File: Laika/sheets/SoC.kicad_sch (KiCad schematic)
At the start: 2 parts, among them J6 Conn_01x03, U1 Milk-V Duo Module

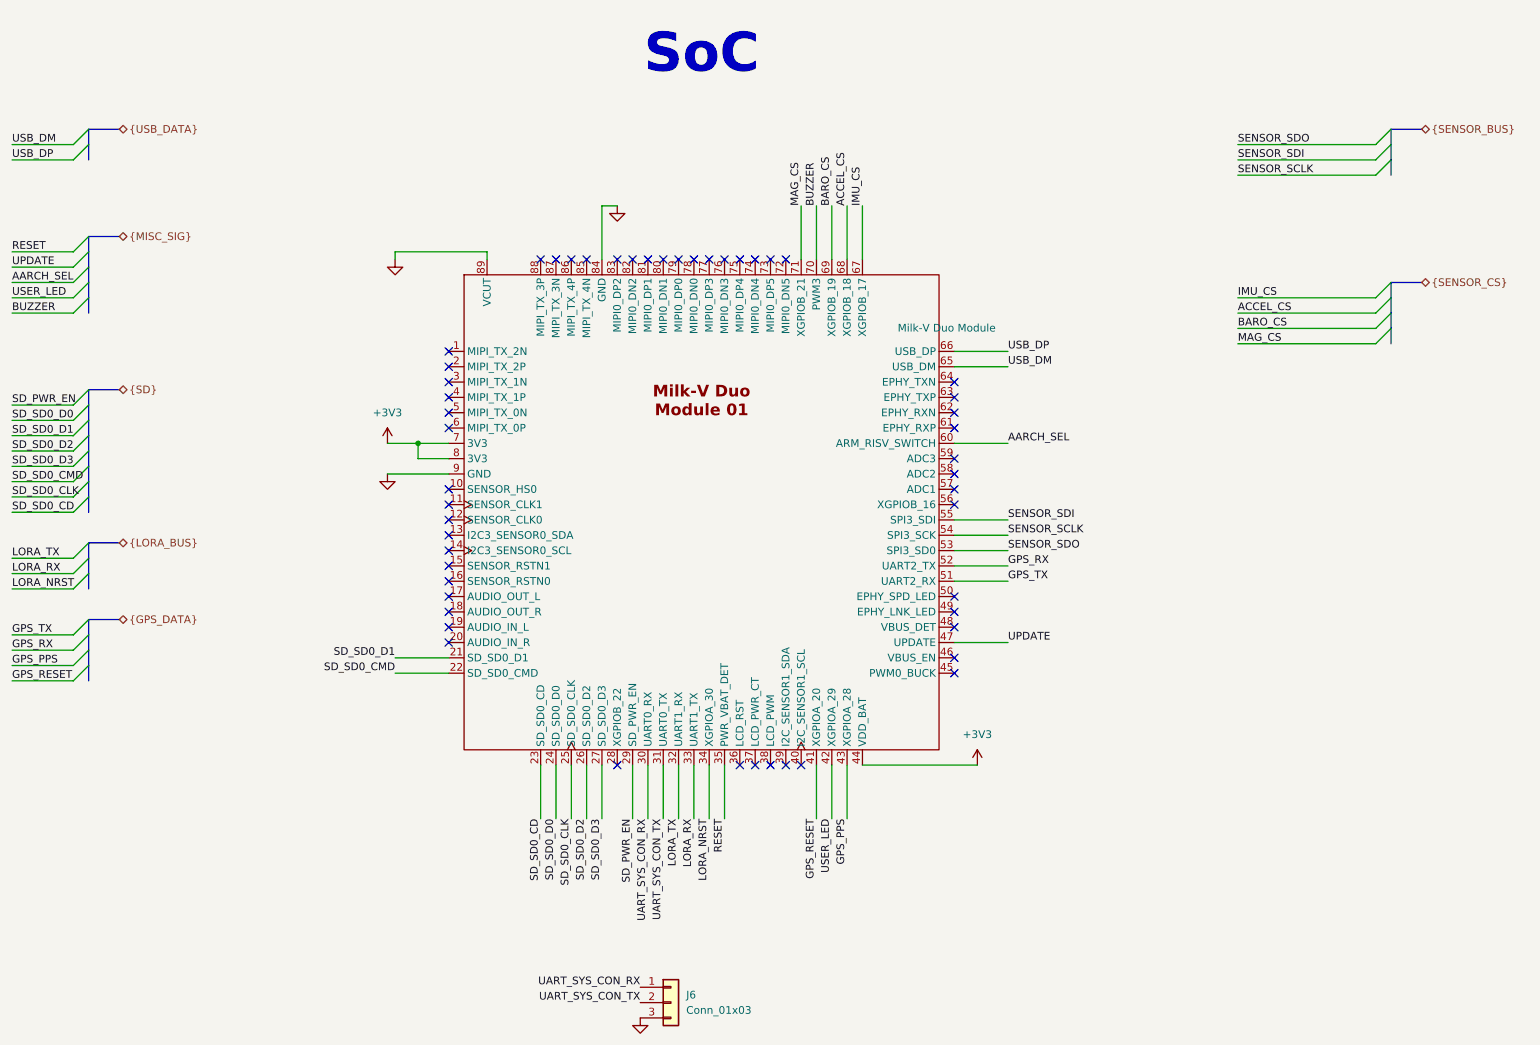
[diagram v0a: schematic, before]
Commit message: Added external GPIO's for user use
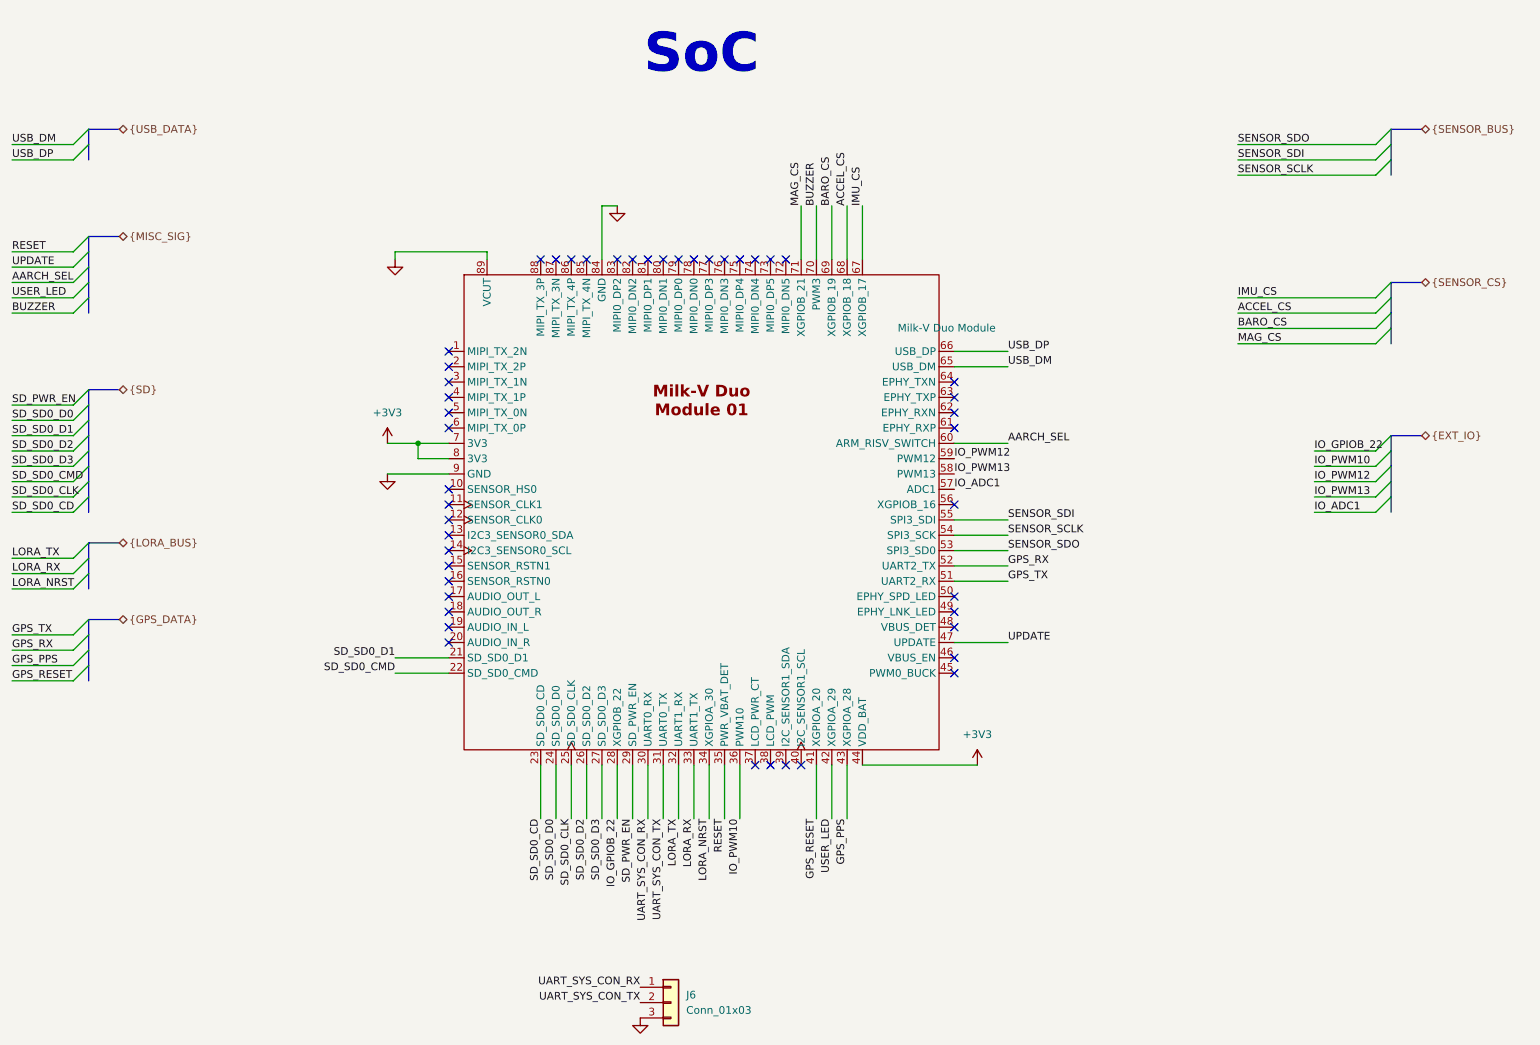
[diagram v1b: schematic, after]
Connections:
- net IO_GPIOB_22: now reaches U1.28 (XGPIOB_22)
- net IO_PWM10: now reaches U1.36 (LCD_RST)
- net IO_ADC1: now reaches U1.57 (ADC1)
- net IO_PWM13: now reaches U1.58 (ADC2)
- net IO_PWM12: now reaches U1.59 (ADC3)
- no-connect marks 52 -> 47

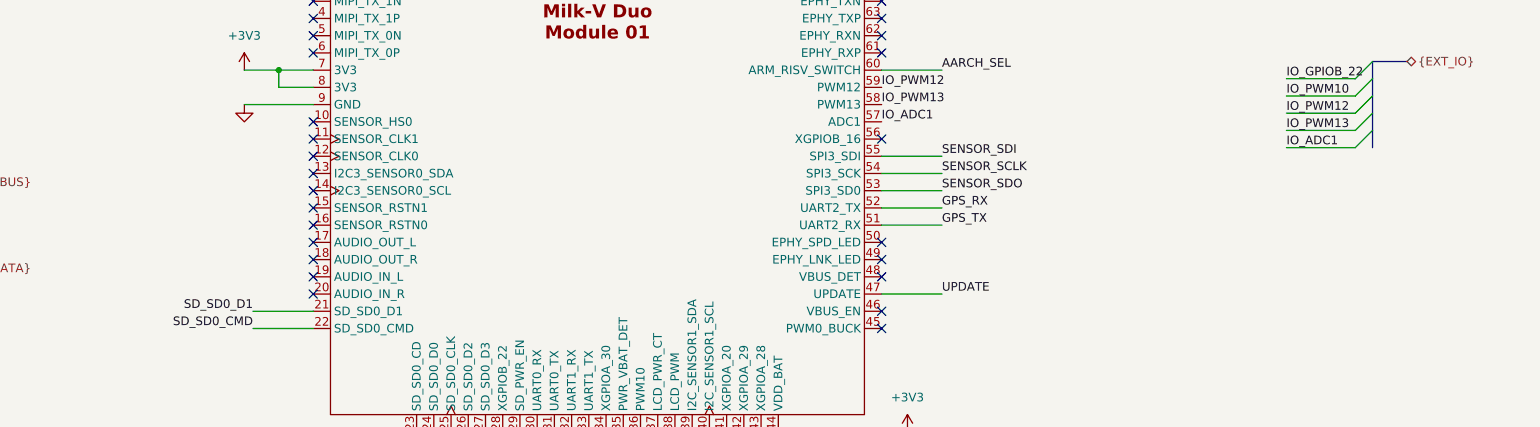
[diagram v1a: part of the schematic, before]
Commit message: Added breakout for I2C as external bus
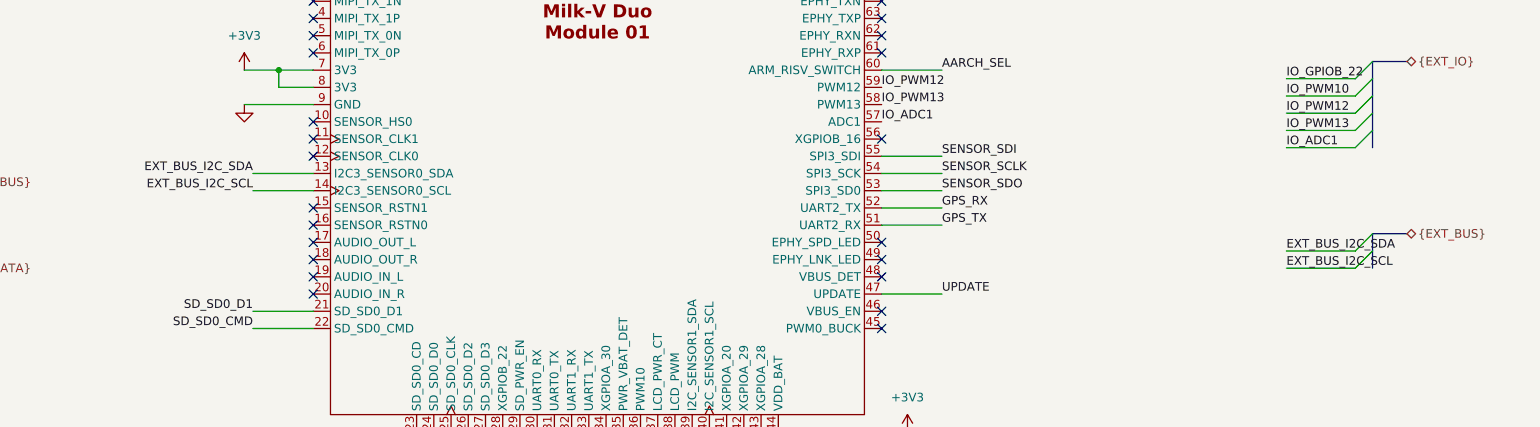
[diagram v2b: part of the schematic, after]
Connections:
- net EXT_BUS_I2C_SDA: now reaches U1.13 (I2C3_SENSOR0_SDA)
- net EXT_BUS_I2C_SCL: now reaches U1.14 (I2C3_SENSOR0_SCL)
- no-connect marks 47 -> 45
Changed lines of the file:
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@@
 		(comment 1 "${VARIANT}")
+	)
+	(bus_alias "EXT_BUS"
+		(members "SENSOR_SD0" "SENSOR_SDI" "SENSOR_SCLK" "EXT_BUS_I2C_SDA" "EXT_BUS_I2C_SCL")
 	)
 	(text "SoC"
@@
 	)
 	(no_connect
-		(at 97.79 107.95)
-	)
-	(no_connect
 		(at 97.79 123.19)
 	)
@@
 	)
 	(no_connect
-		(at 97.79 105.41)
-	)
-	(no_connect
 		(at 135.89 59.69)
 	)
@@
 	)
 	(bus_entry
+		(at 254 116.84)
+		(size -2.54 2.54)
+		(stroke
+			(width 0)
+			(type default)
+		)
+	)
+	(bus_entry
 		(at 254 43.18)
 		(size -2.54 2.54)
@@
 	)
 	(bus_entry
+		(at 254 114.3)
+		(size -2.54 2.54)
+		(stroke
+			(width 0)
+			(type default)
+		)
+	)
+	(bus_entry
 		(at 254 91.44)
 		(size -2.54 2.54)
@@
 		)
 	)
+	(bus
+		(pts
+			(xy 254 116.84) (xy 254 119.38)
+		)
+		(stroke
+			(width 0)
+			(type default)
+		)
+	)
 	(wire
 		(pts
@@
 	(wire
 		(pts
+			(xy 241.3 116.84) (xy 251.46 116.84)
+		)
+		(stroke
+			(width 0)
+			(type default)
+		)
+	)
+	(wire
+		(pts
 			(xy 25.4 86.36) (xy 35.56 86.36)
 		)
@@
 	(wire
 		(pts
+			(xy 88.9 107.95) (xy 97.79 107.95)
+		)
+		(stroke
+			(width 0)
+			(type default)
+		)
+	)
+	(wire
+		(pts
 			(xy 146.05 152.4) (xy 146.05 143.51)
 		)
@@
 		)
 	)
+	(wire
+		(pts
+			(xy 88.9 105.41) (xy 97.79 105.41)
+		)
+		(stroke
+			(width 0)
+			(type default)
+		)
+	)
 	(bus
 		(pts
@@
 	(bus
 		(pts
+			(xy 259.08 114.3) (xy 254 114.3)
+		)
+		(stroke
+			(width 0)
+			(type default)
+		)
+	)
+	(bus
+		(pts
 			(xy 43.18 106.68) (xy 38.1 106.68)
 		)
@@
 		)
 	)
+	(bus
+		(pts
+			(xy 254 114.3) (xy 254 116.84)
+		)
+		(stroke
+			(width 0)
+			(type default)
+		)
+	)
 	(wire
 		(pts
@@
 		(pts
 			(xy 38.1 40.64) (xy 38.1 43.18)
+		)
+		(stroke
+			(width 0)
+			(type default)
+		)
+	)
+	(wire
+		(pts
+			(xy 241.3 119.38) (xy 251.46 119.38)
 		)
 		(stroke
@@
 		)
 	)
+	(label "EXT_BUS_I2C_SDA"
+		(at 241.3 116.84 0)
+		(effects
+			(font
+				(size 1.27 1.27)
+			)
+			(justify left bottom)
+		)
+	)
 	(label "SD_SD0_D0"
 		(at 25.4 86.36 0)
@@
 		)
 	)
+	(label "EXT_BUS_I2C_SCL"
+		(at 88.9 107.95 180)
+		(effects
+			(font
+				(size 1.27 1.27)
+			)
+			(justify right bottom)
+		)
+	)
 	(label "IO_PWM13"
 		(at 181.61 95.25 0)
@@
 		)
 	)
+	(label "EXT_BUS_I2C_SDA"
+		(at 88.9 105.41 180)
+		(effects
+			(font
+				(size 1.27 1.27)
+			)
+			(justify right bottom)
+		)
+	)
 	(label "GPS_RX"
 		(at 190.5 110.49 0)
@@
 		)
 	)
+	(label "EXT_BUS_I2C_SCL"
+		(at 241.3 119.38 0)
+		(effects
+			(font
+				(size 1.27 1.27)
+			)
+			(justify left bottom)
+		)
+	)
 	(label "SD_SD0_D1"
 		(at 88.9 125.73 180)
@@
 		)
 	)
+	(hierarchical_label "{EXT_BUS}"
+		(shape bidirectional)
+		(at 259.08 114.3 0)
+		(effects
+			(font
+				(size 1.27 1.27)
+			)
+			(justify left)
+		)
+	)

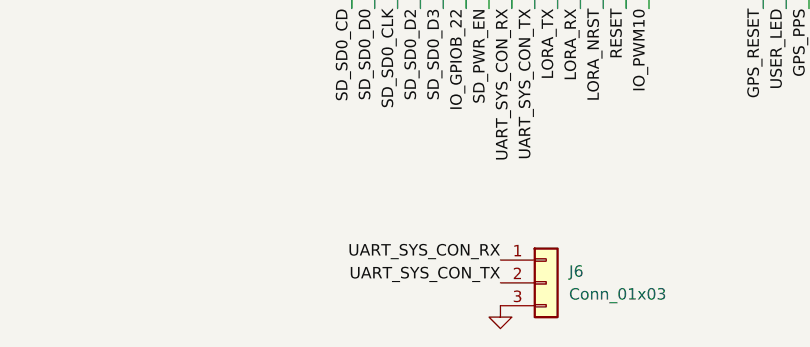
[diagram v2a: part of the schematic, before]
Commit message: Populated BOM with part numbers and footprints
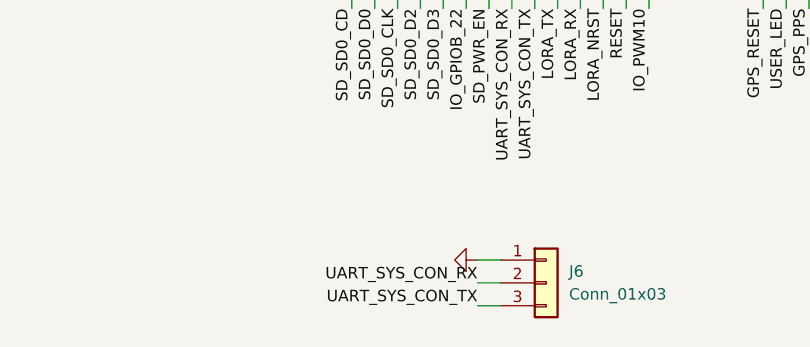
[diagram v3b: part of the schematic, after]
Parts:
- J6: footprint (none) -> Connector_PinHeader_1.00mm:PinHeader_1x03_P1.00mm_Vertical
- U1: JLC Part Type (none) -> N/A; Manafacturer (none) -> Milk-V; Part Number (none) -> Duo Module 01
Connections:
- net GND: now also J6.1 (Pin_1); no longer J6.3 (Pin_3)
- net UART_SYS_CON_RX: now also J6.2 (Pin_2); no longer J6.1 (Pin_1)
- net UART_SYS_CON_TX: now also J6.3 (Pin_3); no longer J6.2 (Pin_2)
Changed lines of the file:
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@@
+	(wire
+		(pts
+			(xy 127 180.34) (xy 129.54 180.34)
+		)
+		(stroke
+			(width 0)
+			(type default)
+		)
+	)
 	(wire
 		(pts
@@
 		)
 	)
+	(wire
+		(pts
+			(xy 127 185.42) (xy 129.54 185.42)
+		)
+		(stroke
+			(width 0)
+			(type default)
+		)
+	)
 	(bus
 		(pts
@@
 		(pts
 			(xy 25.4 68.58) (xy 35.56 68.58)
+		)
+		(stroke
+			(width 0)
+			(type default)
+		)
+	)
+	(wire
+		(pts
+			(xy 127 182.88) (xy 129.54 182.88)
 		)
 		(stroke
@@
 		)
 	)
+	(label "UART_SYS_CON_TX"
+		(at 127 185.42 180)
+		(effects
+			(font
+				(size 1.27 1.27)
+			)
+			(justify right bottom)
+		)
+	)
 	(label "LORA_RX"
 		(at 25.4 111.76 0)
@@
 		)
 	)
+	(label "UART_SYS_CON_RX"
+		(at 127 182.88 180)
+		(effects
+			(font
+				(size 1.27 1.27)
+			)
+			(justify right bottom)
+		)
+	)
 	(label "SENSOR_SDO"
 		(at 228.6 40.64 0)
@@
 		)
 	)
-	(label "UART_SYS_CON_TX"
-		(at 129.54 182.88 180)
-		(effects
-			(font
-				(size 1.27 1.27)
-			)
-			(justify right bottom)
-		)
-	)
 	(label "EXT_BUS_I2C_SDA"
 		(at 241.3 116.84 0)
@@
 	(label "SD_PWR_EN"
 		(at 128.27 152.4 270)
-		(effects
-			(font
-				(size 1.27 1.27)
-			)
-			(justify right bottom)
-		)
-	)
-	(label "UART_SYS_CON_RX"
-		(at 129.54 180.34 180)
 		(effects
 			(font
@@
 	(symbol
 		(lib_id "power:GND")
-		(at 129.54 185.42 0)
+		(at 127 180.34 270)
 		(unit 1)
 		(exclude_from_sim no)
@@
 		(fields_autoplaced yes)
 		(property "Reference" "#PWR059"
-			(at 129.54 191.77 0)
+			(at 120.65 180.34 0)
 			(effects
 				(font
@@
 		)
 		(property "Value" "GND"
-			(at 129.54 190.5 0)
+			(at 121.92 180.34 0)
 			(effects
 				(font
@@
 		)
 		(property "Footprint" ""
-			(at 129.54 185.42 0)
+			(at 127 180.34 0)
 			(effects
 				(font
@@
 		)
 		(property "Datasheet" ""
-			(at 129.54 185.42 0)
+			(at 127 180.34 0)
 			(effects
 				(font
@@
 		)
 		(property "Description" "Power symbol creates a global label with name \"GND\" , ground"
-			(at 129.54 185.42 0)
+			(at 127 180.34 0)
 			(effects
 				(font
@@
 			)
 		)
-		(property "JLC Part Type" ""
+		(property "JLC Part Type" "N/A"
 			(at 139.7 101.6 0)
 			(effects
@@
 			)
 		)
-		(property "Part Number" ""
+		(property "Part Number" "Duo Module 01"
 			(at 139.7 101.6 0)
 			(effects
@@
 			)
 		)
-		(property "Manafacturer" ""
+		(property "Manafacturer" "Milk-V"
 			(at 139.7 101.6 0)
 			(effects
@@
 			)
 		)
-		(property "Footprint" ""
+		(property "Footprint" "Connector_PinHeader_1.00mm:PinHeader_1x03_P1.00mm_Vertical"
 			(at 134.62 182.88 0)
 			(effects

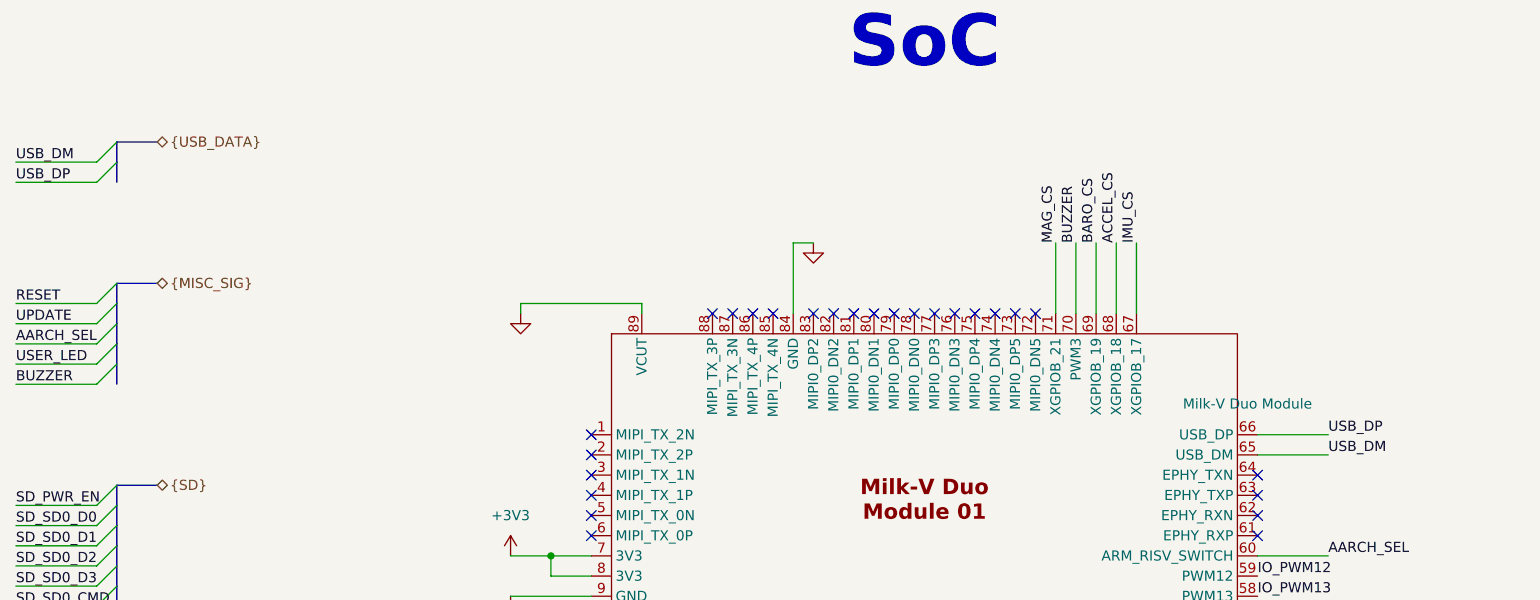
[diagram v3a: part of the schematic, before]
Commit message: Rename USB_DM to USB_DN
Matches KiCad Differential Naming Conventian
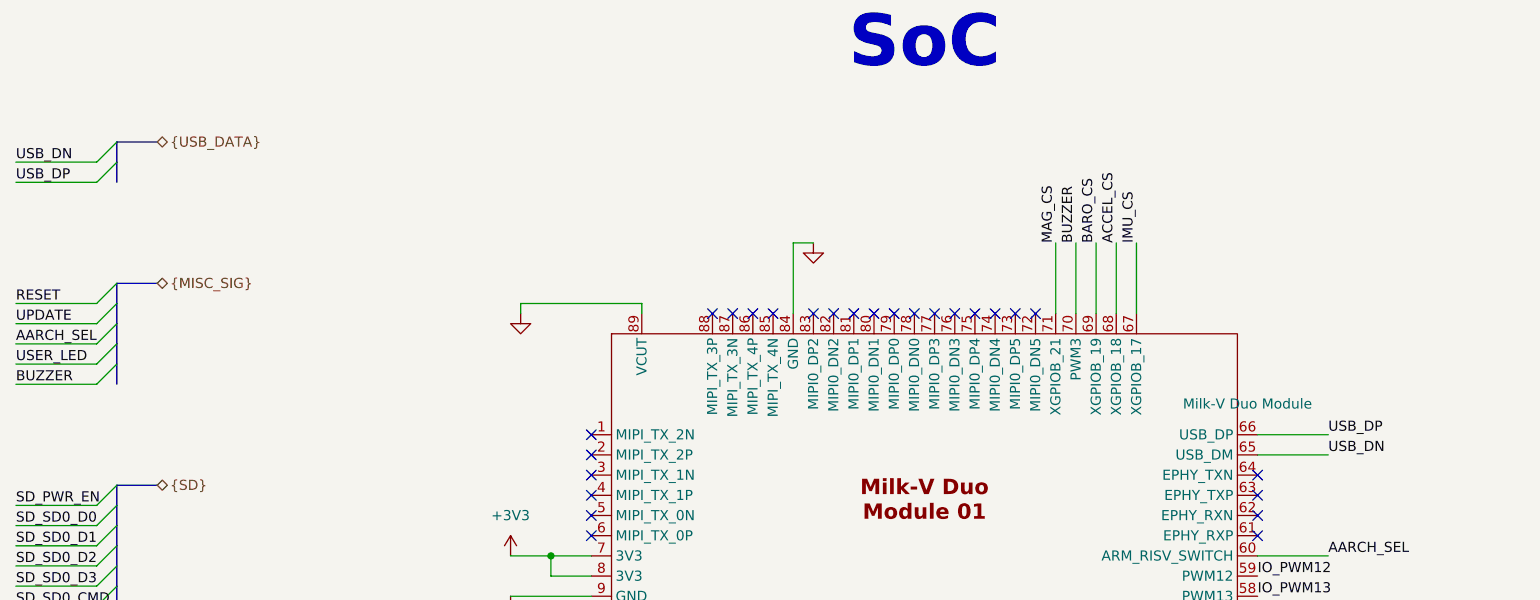
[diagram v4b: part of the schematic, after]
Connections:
- net USB_DM renamed USB_DN
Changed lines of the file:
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@@
 		)
 	)
-	(label "USB_DM"
+	(label "USB_DN"
 		(at 190.5 77.47 0)
 		(effects
@@
 		)
 	)
-	(label "USB_DM"
+	(label "USB_DN"
 		(at 25.4 40.64 0)
 		(effects
